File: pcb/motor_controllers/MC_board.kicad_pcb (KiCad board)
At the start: 2 copper layers, 110.5 x 130.8 mm, 35 parts, among them J12V1 Screw_Terminal_01x02, J12V2 Screw_Terminal_01x02, J12V3 Screw_Terminal_01x02, J12V4 Screw_Terminal_01x02, J2 RJ45, J5V1 Screw_Terminal_01x02, J5V2 Screw_Terminal_01x02, J9V1 Screw_Terminal_01x02, U1 Teensy3.2, U2 MAX98306

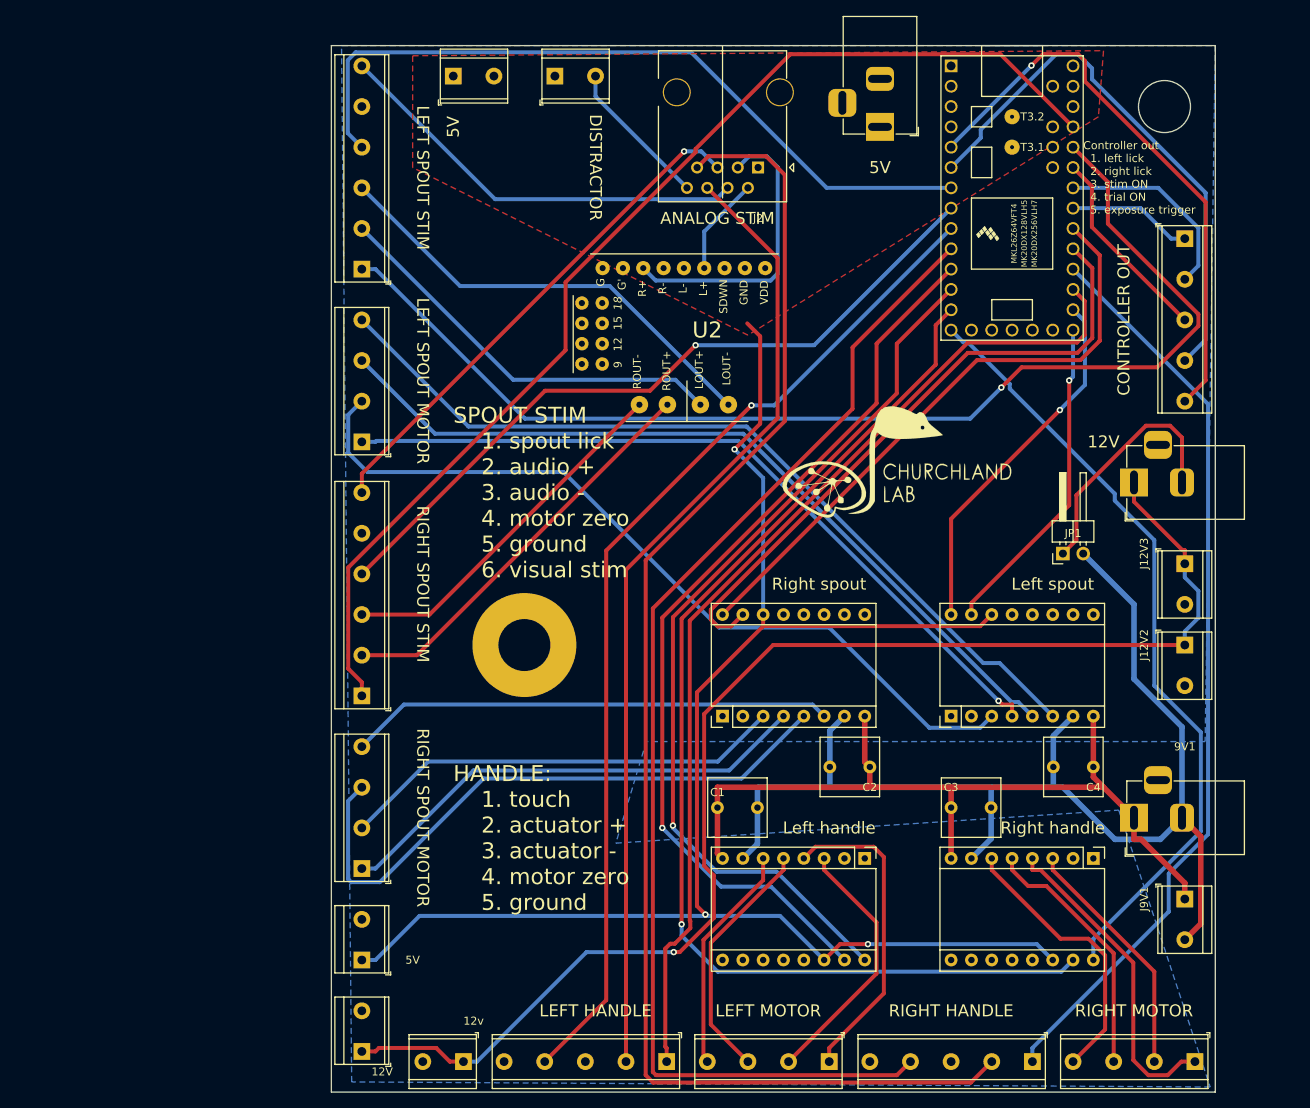
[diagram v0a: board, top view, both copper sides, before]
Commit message: Flipped motor controller for space, added switches
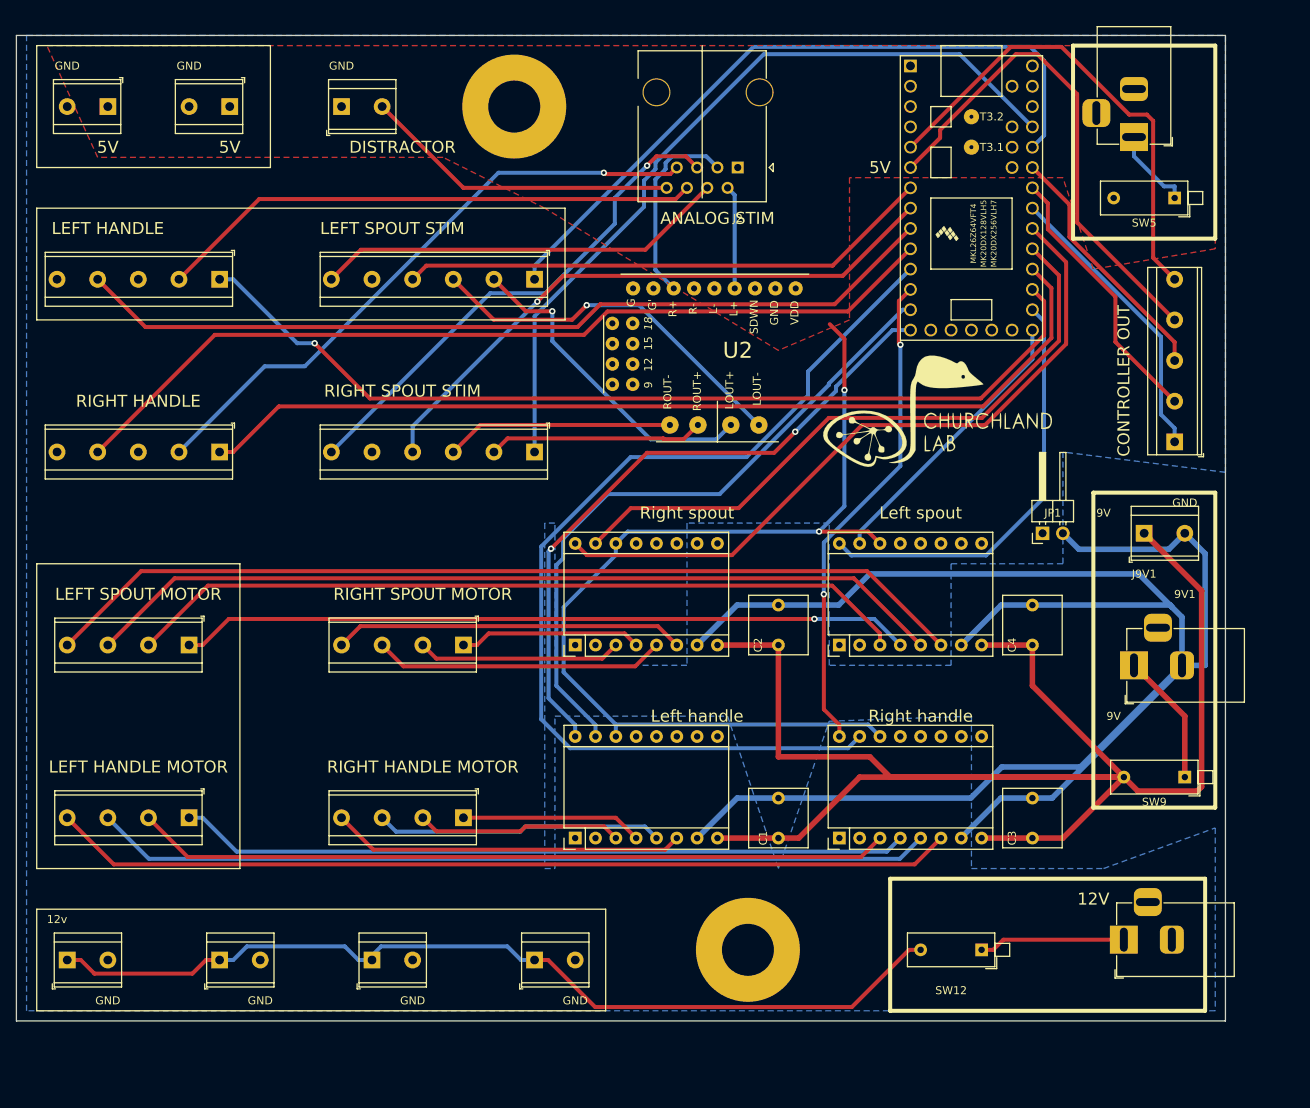
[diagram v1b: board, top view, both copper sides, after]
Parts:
- added SW12: SW12V, Button_Switch_THT:SW_DIP_SPSTx01_Piano_10.8x4.1mm_W7.62mm_P2.54mm, F.Cu at (114.3, 143.5)
- added SW5: SW5V, Button_Switch_THT:SW_DIP_SPSTx01_Piano_10.8x4.1mm_W7.62mm_P2.54mm, F.Cu at (138.4, 49.5)
- added SW9: SW9V, Button_Switch_THT:SW_DIP_SPSTx01_Piano_10.8x4.1mm_W7.62mm_P2.54mm, F.Cu at (139.7, 121.9)
- mount1: value MountingHole_6.5mm -> MountingHole_6.5mm_Pad; footprint MountingHole:MountingHole_6.5mm -> MountingHole:MountingHole_6.5mm_Pad
- moved ToHandleR1 127.0 mm to (19.1, 81.3)
- moved ToHandleL1 112.6 mm to (19.1, 59.7)
- moved J12V2 109.0 mm to (38.1, 144.8), turned to 0 degrees
- moved J5V2 108.0 mm to (20.3, 38.1), turned to 180 degrees
- moved HandleR-ToMotor1 96.4 mm to (49.5, 127.0)
- moved J12V3 95.2 mm to (58.4, 144.8), turned to 0 degrees
- moved HandleL-ToMotor1 85.6 mm to (15.2, 127.0)
- moved mount1 81.3 mm to (55.9, 38.1)
- moved MC-LeverR1 64.8 mm to (63.5, 129.5), turned to 90 degrees
- moved 12V1 57.2 mm to (132.1, 142.2)
- moved mount2 47.2 mm to (85.1, 143.5)
- moved J9V1 46.0 mm to (134.6, 91.4), turned to 0 degrees
- moved J5V1 43.3 mm to (5.08, 38.1), turned to 180 degrees
- moved J12V4 38.6 mm to (0.00, 144.8), turned to 0 degrees
- moved SoundVisionR1 37.4 mm to (58.4, 81.3), turned to 180 degrees
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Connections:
- 12V1 pad 1: +12V -> Net-(12V1-Pad1)
- 5V1 pad 1: +5V -> Net-(5V1-Pad1)
- 9V1 pad 1: +9V -> Net-(9V1-Pad1)
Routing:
- net +9V: track 103.6 -> 213.6 mm
- net Net-(J2-Pad7): track 177.0 -> 77.1 mm, vias 0 -> 1
- net GND1: track 151.2 -> 244.7 mm
- net Net-(HandleL-ToMotor1-Pad4): track 28.7 -> 113.0 mm
- net +5V: track 203.2 -> 125.4 mm, vias 3 -> 2
- net Net-(HandleL-ToMotor1-Pad3): track 31.1 -> 104.8 mm
- net Net-(HandleL-ToMotor1-Pad2): track 32.7 -> 94.5 mm
- net Net-(MC-LeverR1-Pad15): track 143.6 -> 82.5 mm, vias 1 -> 0
- net Net-(SoundVisionL1-Pad1): track 145.9 -> 88.9 mm, vias 1 -> 0
- net Net-(J2-Pad6): track 120.7 -> 68.2 mm
- net Net-(HandleL-ToMotor1-Pad1): track 39.5 -> 91.4 mm
- net Net-(MC-LeverL1-Pad16): track 112.5 -> 61.3 mm, vias 1 -> 2
- net +12V: track 166.5 -> 116.9 mm, vias 1 -> 0
- net Net-(SoundVisionR1-Pad1): track 142.9 -> 98.9 mm
- net Net-(MC-SpoutR1-Pad5): track 77.9 -> 36.5 mm
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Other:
- board size 110.5 x 130.8 mm -> 151.1 x 123.2 mm
- board text added: "9V"
- board text added: "GND"
- board text added: "LEFT HANDLE MOTOR"
- board text added: "RIGHT HANDLE MOTOR"
- board text removed: "LEFT MOTOR"
- board text removed: "RIGHT MOTOR"

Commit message: Added text for motor wire colors
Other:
- board text added: "Blue - Red - Green - Black"

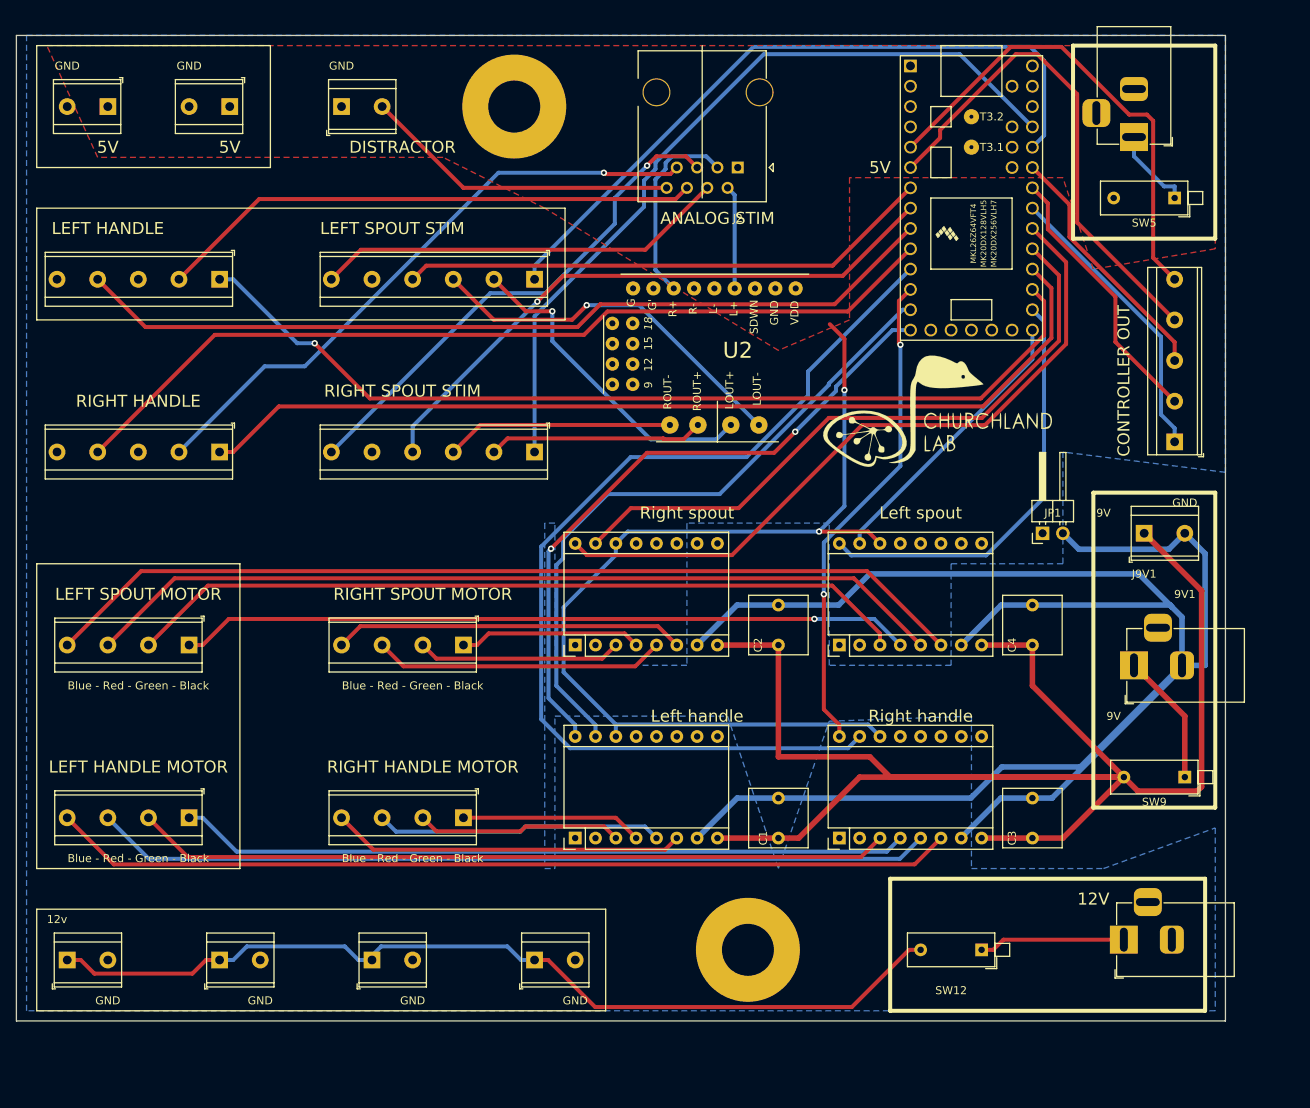
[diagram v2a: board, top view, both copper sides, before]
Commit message: Added switch footprint. Updated wiring.
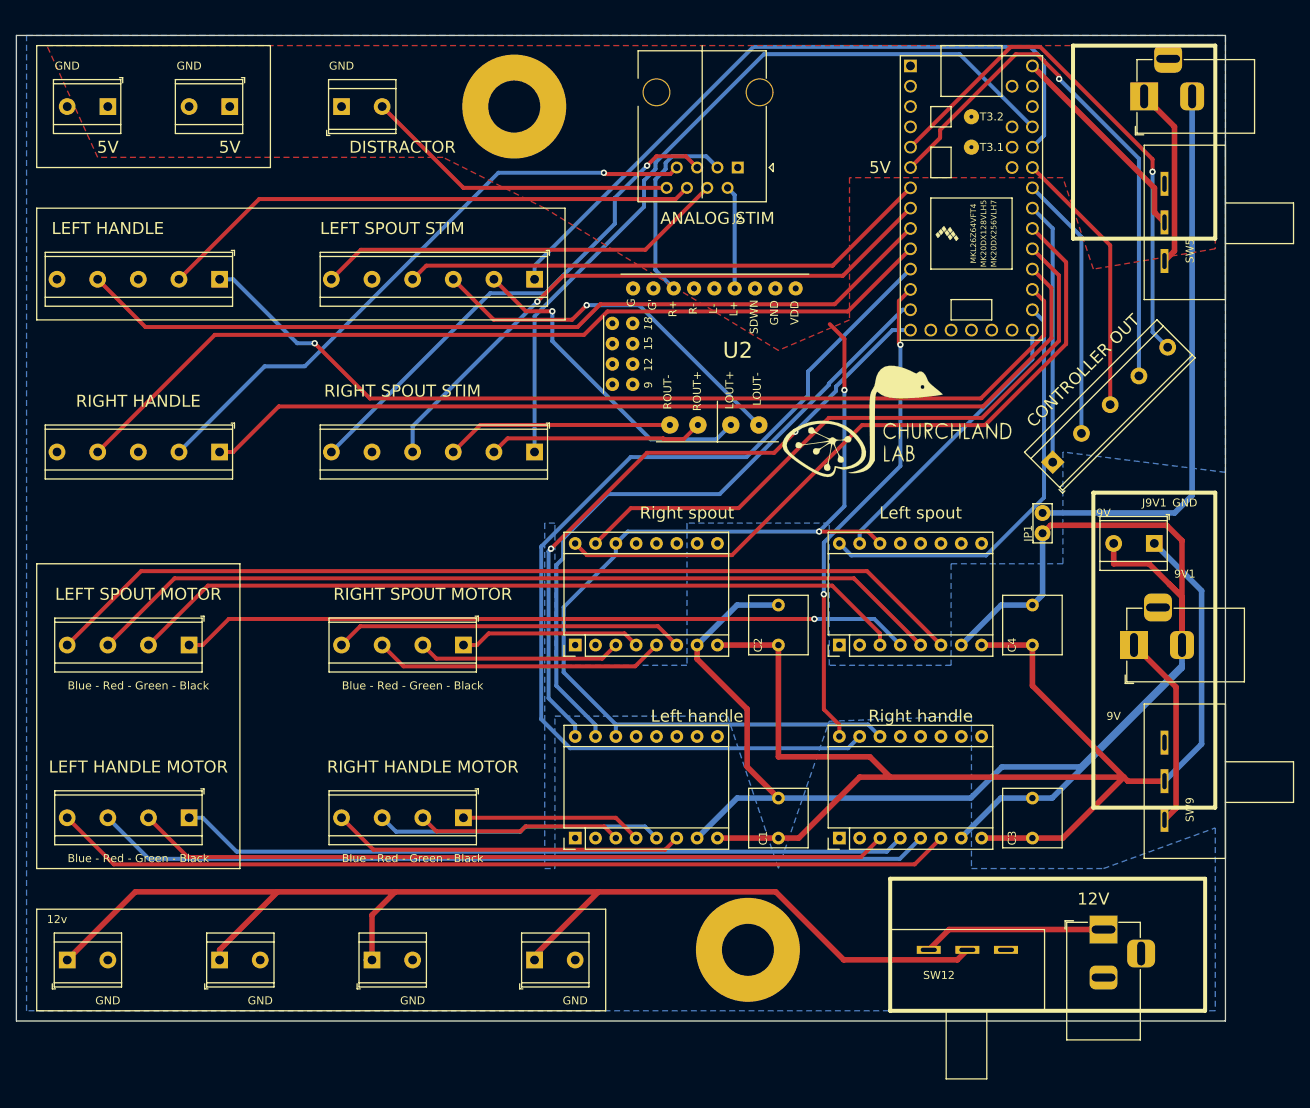
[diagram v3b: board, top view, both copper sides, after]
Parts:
- JP1: footprint Connector_PinHeader_2.54mm:PinHeader_1x02_P2.54mm_Horizontal -> TestPoint:TestPoint_Bridge_Pitch2.54mm_Drill1.0mm
- SW12, SW5, SW9: footprint Button_Switch_THT:SW_DIP_SPSTx01_Piano_10.8x4.1mm_W7.62mm_P2.54mm -> teensy:SW_L102021ML04Q
- moved sync_trigger_out1 15.5 mm to (123.2, 82.5), turned to 45 degrees
- moved SW5 13.3 mm to (134.6, 62.2), turned to 90 degrees
- moved SW12 11.7 mm to (102.9, 141.0), turned to 0 degrees
- moved SW9 11.4 mm to (134.6, 132.1), turned to 90 degrees
- moved 5V1 5.24 mm to (134.6, 36.8), turned to 180 degrees
- moved G*** 5.24 mm to (104.1, 77.5)
- moved 12V1 2.84 mm to (129.5, 141.0), turned to 90 degrees
- moved 9V1 2.54 mm to (133.3, 105.4)
- moved J9V1 1.80 mm to (135.9, 92.7), turned to 180 degrees
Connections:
- JP1 pad 1: GND -> GND1
- JP1 pad 2: GND1 -> GND
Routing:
- net GND: track 0.00 -> 69.5 mm
- net +12V: track 116.9 -> 154.0 mm
- net +9V: track 213.6 -> 178.5 mm
- net GND1: track 244.7 -> 217.6 mm
- net +5V: track 125.4 -> 151.8 mm
- net Net-(5V1-Pad1): track 10.5 -> 22.7 mm
- net Net-(9V1-Pad1): track 16.6 -> 24.6 mm
- net Net-(U1-Pad5): track 60.3 -> 65.5 mm, vias 0 -> 1
- net Net-(U1-Pad6): track 62.6 -> 67.8 mm, vias 0 -> 1
- net Net-(12V1-Pad1): track 18.3 -> 22.9 mm
- net Net-(U1-Pad26): track 36.6 -> 32.8 mm
- net Net-(U1-Pad28): track 31.5 -> 33.7 mm
- net Net-(U1-Pad27): track 34.0 -> 33.2 mm

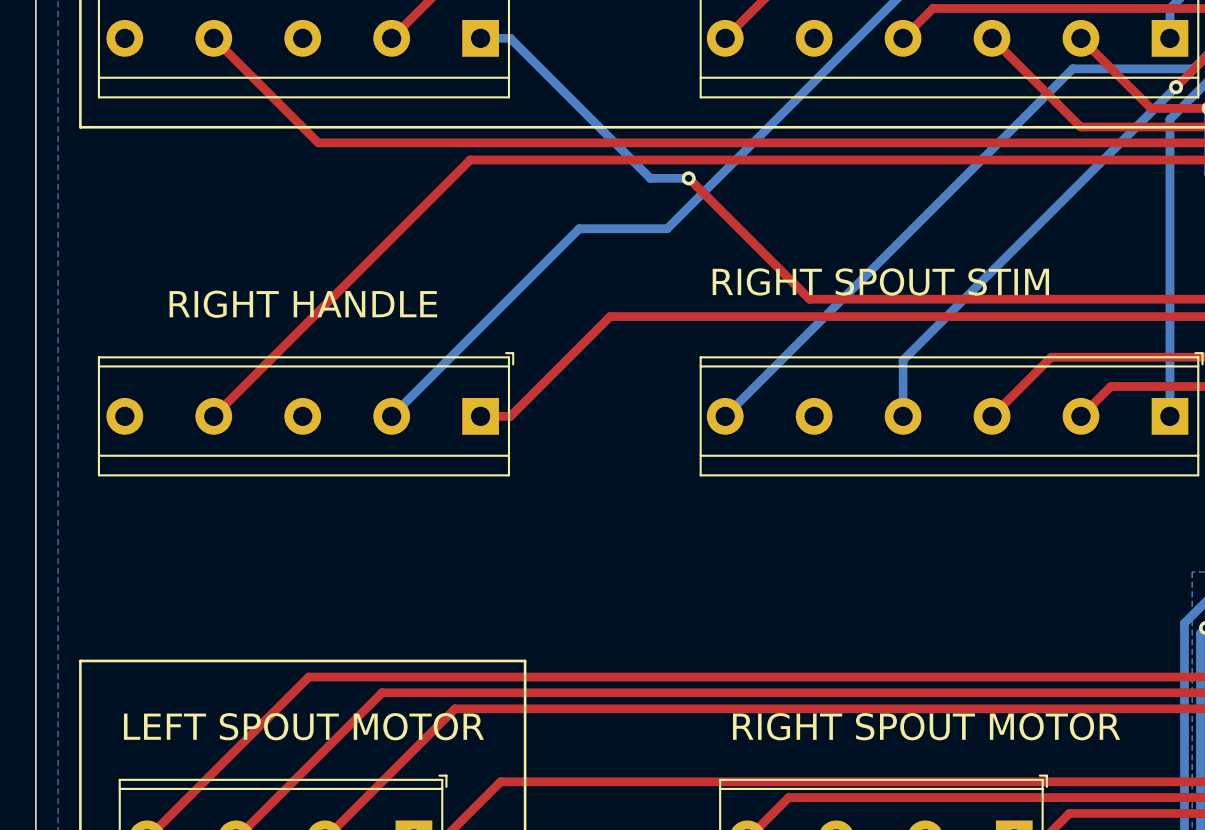
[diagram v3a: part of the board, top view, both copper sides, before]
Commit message: text for handles and spouts
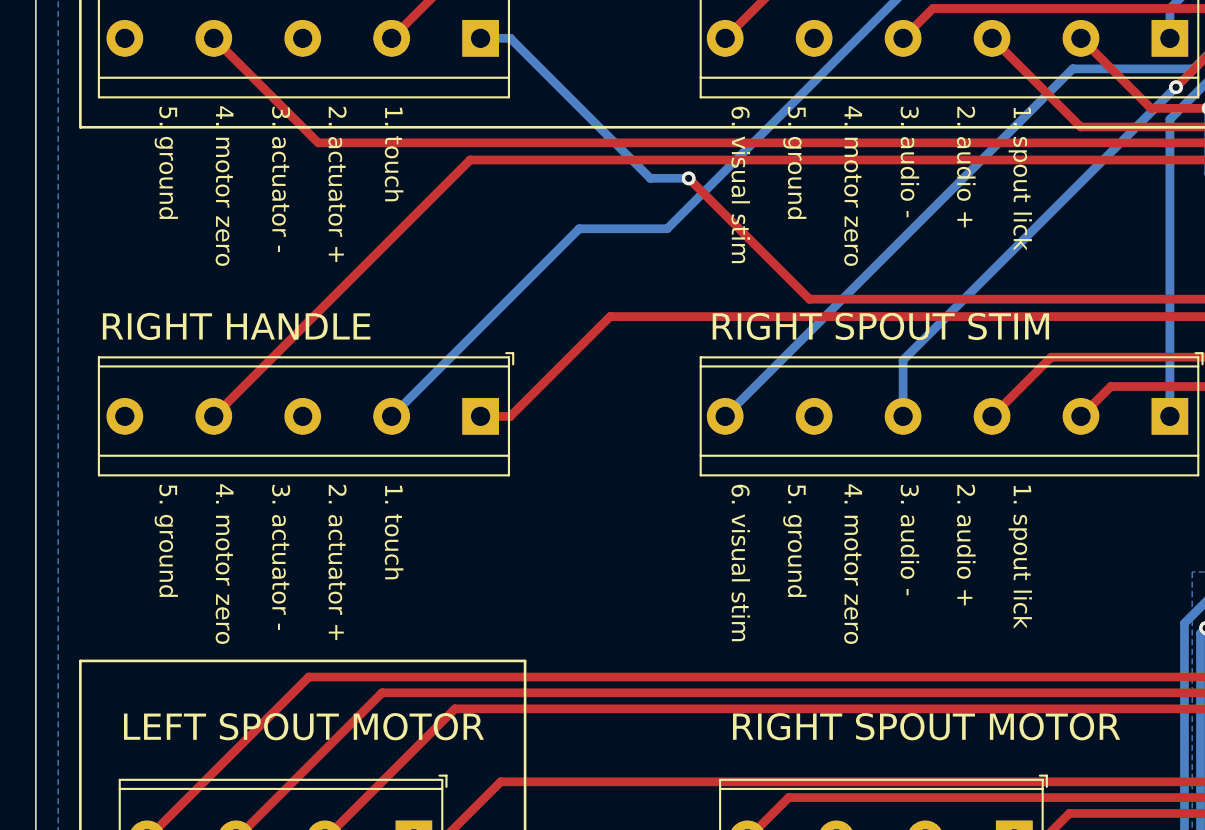
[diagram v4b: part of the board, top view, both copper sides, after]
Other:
- board text added: "1. spout lick 2. audio + 3. audio - 4. motor zero 5. ground 6. visual stim"
- board text added: "1. touch 2. actuator + 3. actuator - 4. motor zero 5. ground"
